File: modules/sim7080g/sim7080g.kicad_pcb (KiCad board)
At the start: 4 copper layers, 25.4 x 57.2 mm, 57 parts, among them J1 Conn_Coaxial, J2 Conn_01x08, J3 Conn_01x08, J4 Conn_Coaxial, Q1 NPN, Q2 NPN, Q3 NPN, U1 TXB0108RGY, U2 SIM7080G, U3 NANO SIM XG6P H1.35

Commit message: production
Signed-off-by: Rodney Osodo <socials@rodneyosodo.com>
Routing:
- net GND: track 64.6 -> 11.3 mm, vias 87 -> 61
- net SIM_DATA: track 26.1 -> 16.9 mm, vias 5 -> 2
- net +1V8: track 38.1 -> 29.4 mm, vias 5 -> 3
- net SIM7080G_RING: track 26.7 -> 18.5 mm
- net SIM_RX: track 25.8 -> 20.5 mm
- net +3V3: track 79.6 -> 84.7 mm, vias 9 -> 7
- net Net-(JP2-A): track 12.5 -> 7.89 mm
- net Net-(U3-RST): track 9.70 -> 13.3 mm, vias 1 -> 0
- net SIM_CLK: track 16.4 -> 20.0 mm, vias 3 -> 2
- net RF_ANT: track 16.5 -> 12.9 mm, vias 1 -> 2
- net PWRKEY: track 28.7 -> 25.2 mm, vias 3 -> 2
- net SIM7080G_TX: track 18.9 -> 15.9 mm, vias 2 -> 1
- net SIM_CTS: track 20.2 -> 17.3 mm
- net SIM_RTS: track 21.3 -> 18.6 mm
- net SIM_TX: track 27.1 -> 24.7 mm
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
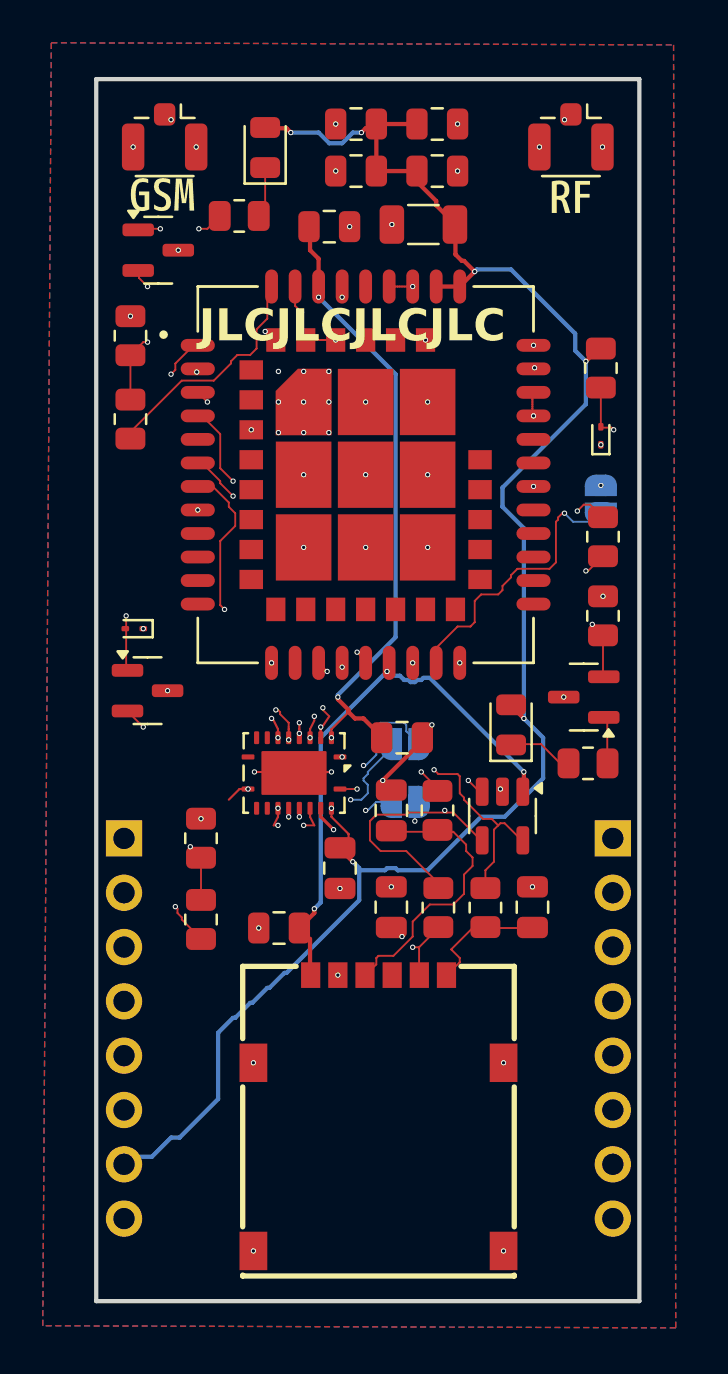
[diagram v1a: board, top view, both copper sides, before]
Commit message: fix: sim7080g module
Signed-off-by: Rodney Osodo <socials@rodneyosodo.com>
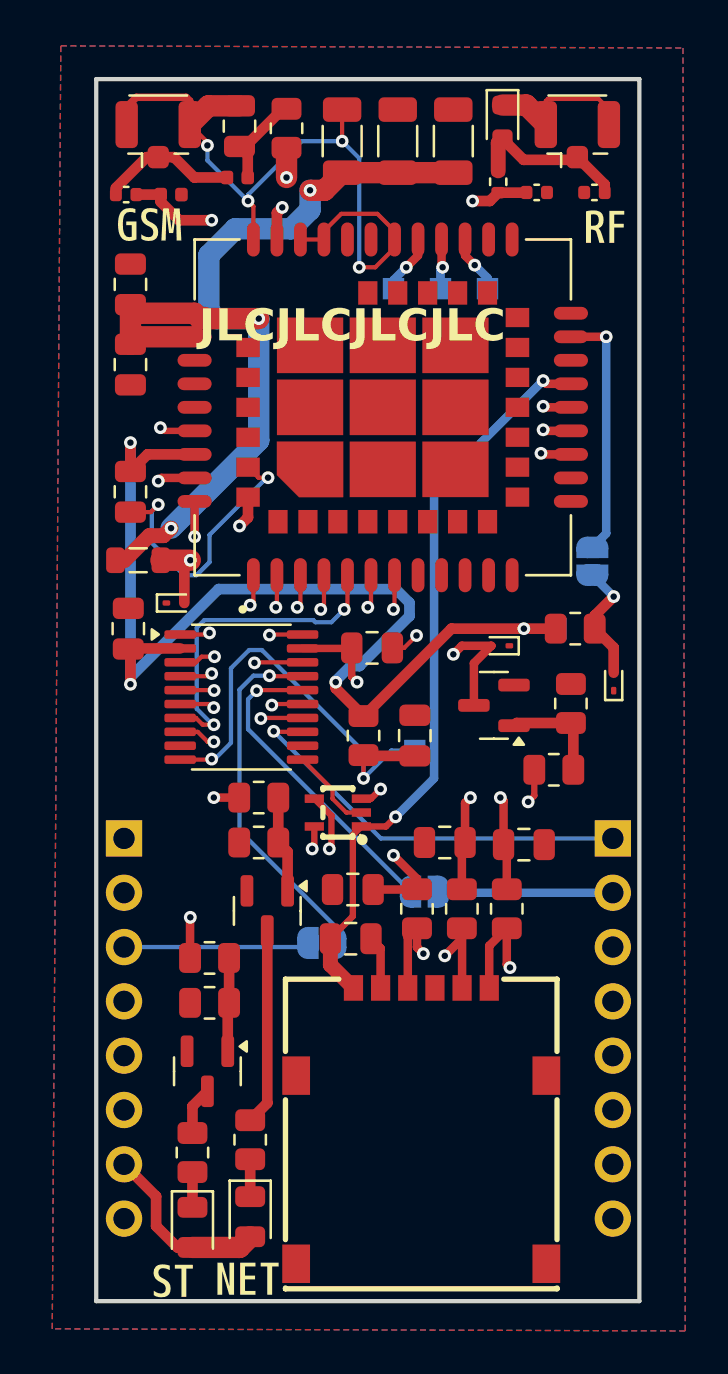
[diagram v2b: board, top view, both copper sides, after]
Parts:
- removed D3: LED, LED_SMD:LED_0805_2012Metric
- removed kibuzzard-6A58AD62: G***, kibuzzard-6A58AD62
- removed kibuzzard-6A58AD87: G***, kibuzzard-6A58AD87
- added C14: 1uF, Capacitor_SMD:C_0805_2012Metric, F.Cu at (93.6, 75.6)
- added C15: 100uF, Capacitor_SMD:C_1206_3216Metric, F.Cu at (103.5, 68.9)
- added C16: 100uF, Capacitor_SMD:C_1206_3216Metric, F.Cu at (106.1, 68.9)
- added C17: 100uF, Capacitor_SMD:C_1206_3216Metric, F.Cu at (108.7, 68.9)
- added C4: 10uF, Capacitor_SMD:C_0805_2012Metric, F.Cu at (93.6, 85.3)
- added D6: ESD9B5.0ST5G, Diode_SMD:D_SOD-923, F.Cu at (95.7, 90.5)
- added D7: LED, LED_SMD:LED_0805_2012Metric, F.Cu at (99.2, 119.2)
- added D8: ESDA6V1W5, modules:C48677, F.Cu at (103.3, 100.3)
- added FB1: FerriteBead, Inductor_SMD:L_0805_2012Metric, F.Cu at (94.0, 88.5)
- added L1: DNP, Inductor_SMD:L_0402_1005Metric, F.Cu at (95.5, 71.4)
- added L2: 47nH, Inductor_SMD:L_0402_1005Metric, F.Cu at (98.6, 70.6)
- added R13: 4.7K, Resistor_SMD:R_0805_2012Metric, F.Cu at (99.6, 99.6)
- added R14: 47K, Resistor_SMD:R_0805_2012Metric, F.Cu at (99.6, 101.7)
- added R15: 680, Resistor_SMD:R_0805_2012Metric, F.Cu at (99.2, 115.6)
- added TP1: TestPoint, TestPoint:TestPoint_Pad_1.0x1.0mm, B.Cu at (106.9, 97.4)
- added TP2: TestPoint, TestPoint:TestPoint_Pad_1.0x1.0mm, B.Cu at (110.3, 75.8)
- added TP3: TestPoint, TestPoint:TestPoint_Pad_1.0x1.0mm, B.Cu at (105.9, 75.8)
- added TP4: TestPoint, TestPoint:TestPoint_Pad_1.0x1.0mm, B.Cu at (108.1, 75.8)
- added TP5: TestPoint, TestPoint:TestPoint_Pad_1.0x1.0mm, B.Cu at (113.5, 91.7)
- added kibuzzard-6AA2AF52: G***, kibuzzard-6AA2AF52, B.Cu at (111.7, 111.7)
- added kibuzzard-6AA2C081: G***, kibuzzard-6AA2C081, F.Cu at (99.1, 122.1)
- added kibuzzard-6AA2C0AA: G***, kibuzzard-6AA2C0AA, F.Cu at (95.6, 122.2)
- added kibuzzard-6AA2C170: G***, kibuzzard-6AA2C170, B.Cu at (108.1, 73.8)
- added kibuzzard-6AA2C182: G***, kibuzzard-6AA2C182, B.Cu at (105.9, 73.8)
- C10: value 0.1uF -> 22pF
- C11: value 0.1uF -> 33pF; footprint Capacitor_SMD:C_0805_2012Metric -> Capacitor_SMD:C_0402_1005Metric
- C12: value 0.1uF -> DNP; footprint Capacitor_SMD:C_0805_2012Metric -> Capacitor_SMD:C_0402_1005Metric
- C3: value 10uF -> 0.1uF
- C6: value 22pF -> 0.1uF
- C8: value 22pF -> DNP; footprint Capacitor_SMD:C_0805_2012Metric -> Capacitor_SMD:C_0402_1005Metric
- C9: value 100uF -> 22pF; footprint Capacitor_SMD:C_1206_3216Metric -> Capacitor_SMD:C_0805_2012Metric
- D2: value ESDA6V1SC5 -> PESD0603V24; footprint Package_TO_SOT_SMD:SOT-23-5 -> Diode_SMD:D_0603_1608Metric
- J1: value Conn_Coaxial -> Conn_01x08; footprint Connector_Coaxial:U.FL_Hirose_U.FL-R-SMT-1_Vertical -> Connector_PinHeader_2.54mm:PinHeader_1x08_P2.54mm_Vertical; moved to B.Cu
- J3: value Conn_01x08 -> Conn_Coaxial; footprint Connector_PinHeader_2.54mm:PinHeader_1x08_P2.54mm_Vertical -> Connector_Coaxial:U.FL_Hirose_U.FL-R-SMT-1_Vertical; moved to F.Cu
- Q1, Q2, Q3: value NPN -> MMBT3904
- R10: value 47K -> 680
- R11: value 47K -> 4.7K
- R12: value 100 -> 47K
- R2: value 4.7K -> 10K
- R3: value 22 -> 10
- R4: value 22 -> 0; footprint Resistor_SMD:R_0805_2012Metric -> Resistor_SMD:R_0402_1005Metric
- R6: value 47K -> 22
- R7: value 100 -> 22
- R9: value 4.7K -> 47K
- U1: value TXB0108RGY -> TXB0108PW; footprint Package_DFN_QFN:Texas_RGY_R-PVQFN-N20_EP2.05x3.05mm -> Package_SO:TSSOP-20_4.4x6.5mm_P0.65mm
- moved J3 39.6 mm to (94.9, 68.1), turned to 90 degrees
- moved Q1 38.5 mm to (97.2, 112.4), turned to -90 degrees
- moved C5 37.5 mm to (98.7, 68.2), turned to -90 degrees
- moved R7 34.7 mm to (111.2, 104.8), turned to -90 degrees
- moved R4 34.1 mm to (110.8, 70.8), turned to 90 degrees
- moved C8 33.4 mm to (112.6, 71.3), turned to 0 degrees
- moved J1 32.9 mm to (93.3, 101.5), turned to 180 degrees
- moved R3 32.7 mm to (100.9, 68.3)
- moved D2 32.5 mm to (111.0, 68.0)
- moved C10 31.8 mm to (112.0, 101.8), turned to 180 degrees
- moved R10 31.6 mm to (96.5, 116.2), turned to -90 degrees
- moved R6 31.0 mm to (109.1, 104.8), turned to -90 degrees
- moved C9 28.9 mm to (108.3, 101.7), turned to 0 degrees
- moved R9 28.5 mm to (97.3, 109.2), turned to 180 degrees
- moved D4 27.8 mm to (96.5, 119.7), turned to -90 degrees
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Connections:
- C1 pad 2: +1V8 -> Net-(U1-OE)
- C10 pad 1: +3V3 -> GND
- C10 pad 2: GND -> SIM_DATA
- C11 pad 1: +3V3 -> Net-(J3-In)
- C11 pad 2: GND -> GNSS_ANT
- C12 pad 1: +3V3 -> Net-(D2-A2)
- C13 pad 1: +3V3 -> GND
- C13 pad 2: GND -> VBAT
- C2 pad 2: +3V3 -> +1V8
- C3 pad 2: +1V8 -> +3V3
- C5 pad 2: SIM_VDD -> V_ANT
- C6 pad 2: Net-(U3-RST) -> SIM_VDD
- C7 pad 2: Net-(U3-CLK) -> SIM_RST
- C8 pad 1: GND -> RF_ANT
- C8 pad 2: Net-(U3-I/O) -> GND
- C9 pad 1: +3V3 -> GND
- C9 pad 2: GND -> SIM_CLK
- D2 pad 1: SIM_VDD -> GND
- D2 pad 2: GND -> Net-(D2-A2)
- J1 pad 1: GNSS_ANT -> SIM7080G_DTR
- J1 pad 2: GND -> SIM7080G_PWR
- J2 pad 1: SIM7080G_DTR -> SIM7080G_RING
- J2 pad 2: SIM7080G_PWR -> SIM7080G_CTS
- J2 pad 3: SIM7080G_RTS -> SIM7080G_TX
- J2 pad 4: unconnected-(J2-Pin_4-Pad4) -> SIM7080G_RX
- J2 pad 5: unconnected-(J2-Pin_5-Pad5) -> SIM7080G_DCD
- J2 pad 7: +3V3 -> unconnected-(J2-Pin_7-Pad7)
- J3 pad 1: SIM7080G_RING -> Net-(J3-In)
- J3 pad 2: SIM7080G_CTS -> GND
- J4 pad 1: RF_ANT -> Net-(D2-A2)
- Q1 pad 1: Net-(Q1-C) -> Net-(Q1-B)
- Q1 pad 2: Net-(Q1-B) -> GND
- Q1 pad 3: GND -> Net-(Q1-C)
- Q2 pad 1: PWRKEY -> Net-(Q2-B)
- Q2 pad 2: Net-(Q2-B) -> GND
- Q2 pad 3: GND -> PWRKEY
- Q3 pad 1: Net-(Q3-C) -> Net-(Q3-B)
- Q3 pad 2: Net-(Q3-B) -> GND
- Q3 pad 3: GND -> Net-(Q3-C)
- R1 pad 1: +3V3 -> +1V8
- R10 pad 1: Net-(Q3-B) -> Net-(Q1-C)
- R10 pad 2: GND -> Net-(D4-K)
- R11 pad 1: Net-(Q2-B) -> SIM7080G_PWR
- R11 pad 2: GND -> Net-(Q2-B)
- R12 pad 1: Net-(Q3-C) -> Net-(Q2-B)
- R12 pad 2: Net-(D4-K) -> GND
- R2 pad 1: STATUS -> Net-(U1-OE)
- R2 pad 2: Net-(Q1-B) -> +1V8
- R3 pad 1: SIM_RST -> V_ANT
- R3 pad 2: Net-(U3-RST) -> +3V3
- R4 pad 1: SIM_CLK -> RF_ANT
- R4 pad 2: Net-(U3-CLK) -> Net-(D2-A2)
- R5 pad 1: SIM_DATA -> SIM_RST
- R5 pad 2: Net-(U3-I/O) -> Net-(U3-RST)
- R6 pad 1: Net-(Q1-B) -> SIM_CLK
- R6 pad 2: GND -> Net-(U3-CLK)
- R7 pad 1: Net-(Q1-C) -> SIM_DATA
- R7 pad 2: Net-(D3-K) -> Net-(U3-I/O)
- R8 pad 1: SIM7080G_PWR -> STATUS
- R8 pad 2: Net-(Q2-B) -> Net-(Q1-B)
- R9 pad 1: NETLIGHT -> Net-(Q1-B)
- R9 pad 2: Net-(Q3-B) -> GND
- U1 pad 10: unconnected-(U1-OE-Pad10) -> Net-(U1-OE)
- U1 pad 12: unconnected-(U1-B8-Pad12) -> GND
- U1 pad 13: unconnected-(U1-B7-Pad13) -> SIM7080G_RING
- U1 pad 14: SIM7080G_RING -> SIM7080G_DCD
- U1 pad 7: SIM_RI -> SIM_DCD
- U1 pad 8: unconnected-(U1-A7-Pad8) -> SIM_RI
- U1 pad 9: unconnected-(U1-A8-Pad9) -> GND
- U2 pad 24: unconnected-(U2-USB_VBUS-Pad24) -> Net-(U2-USB_VBUS)
- U2 pad 25: unconnected-(U2-USB_DP-Pad25) -> Net-(U2-USB_DP)
- U2 pad 26: unconnected-(U2-USB_DM-Pad26) -> Net-(U2-USB_DM)
- U2 pad 34: +3V3 -> VBAT
- U2 pad 35: +3V3 -> VBAT
- U2 pad 5: unconnected-(U2-UART1_DCD-Pad5) -> SIM_DCD
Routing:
- net +3V3: track 84.7 -> 17.4 mm, vias 7 -> 3
- net GND: track 11.3 -> 64.6 mm, vias 61 -> 7
- net VBAT: track 0.00 -> 44.6 mm, vias 0 -> 3
- net SIM7080G_PWR: track 4.69 -> 30.8 mm
- net +1V8: track 29.4 -> 55.2 mm, vias 3 -> 4
- net SIM7080G_DCD: track 0.00 -> 25.0 mm, vias 0 -> 1
- net Net-(U1-OE): track 0.00 -> 22.4 mm, vias 0 -> 2
- net SIM_TX: track 24.7 -> 5.31 mm
- net SIM_RST: track 12.0 -> 29.3 mm, vias 3 -> 2
- net SIM_DCD: track 0.00 -> 15.6 mm, vias 0 -> 2
- net SIM_RX: track 20.5 -> 7.06 mm, vias 3 -> 2
- net Net-(U3-I/O): track 5.92 -> 19.1 mm, vias 0 -> 2
- net Net-(U3-CLK): track 4.31 -> 16.0 mm
- net SIM7080G_RTS: track 19.9 -> 8.68 mm, vias 1 -> 0
- net STATUS: track 11.1 -> 21.9 mm, vias 0 -> 2
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- added copper zone on In1.Cu, net +3V3
